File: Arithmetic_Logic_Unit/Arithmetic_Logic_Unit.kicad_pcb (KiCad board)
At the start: 2 copper layers, 95.9 x 90.2 mm, 5 parts, among them J1 PC104

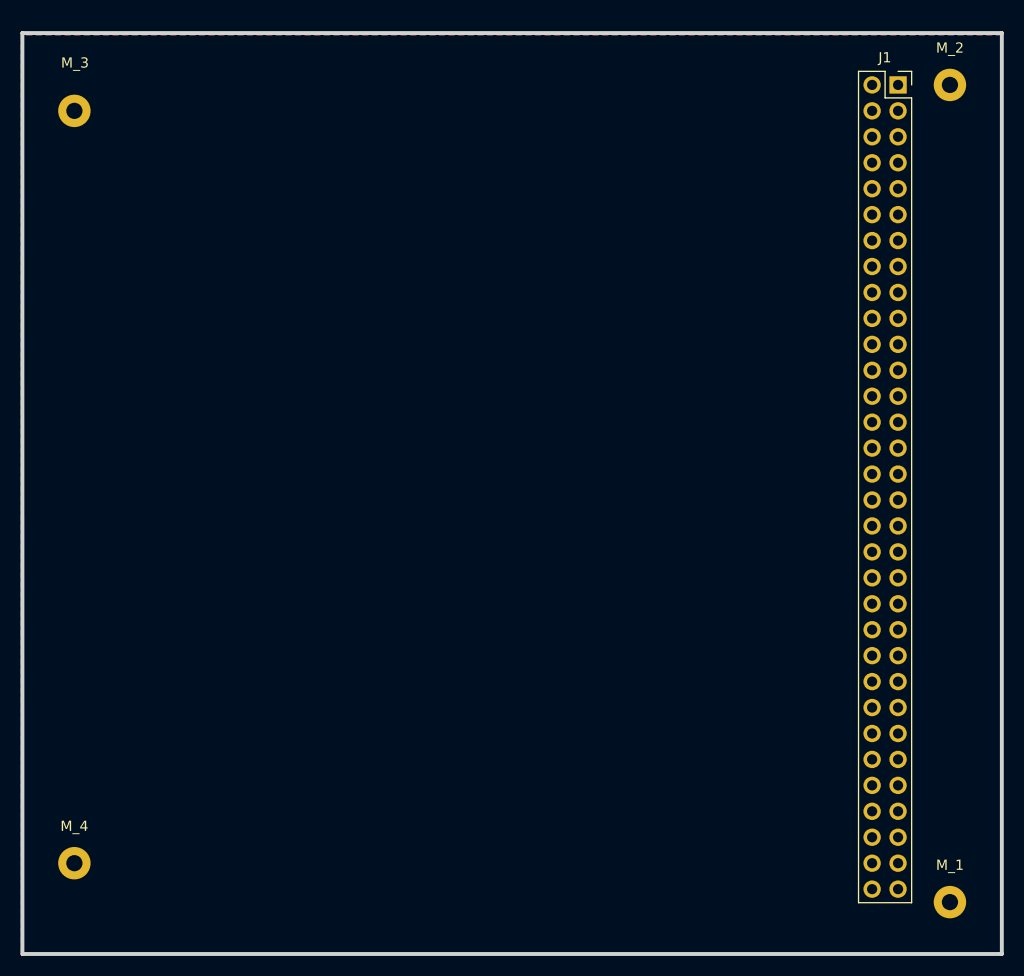
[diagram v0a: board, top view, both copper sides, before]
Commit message: preliminary board layout, will move IR to clock module
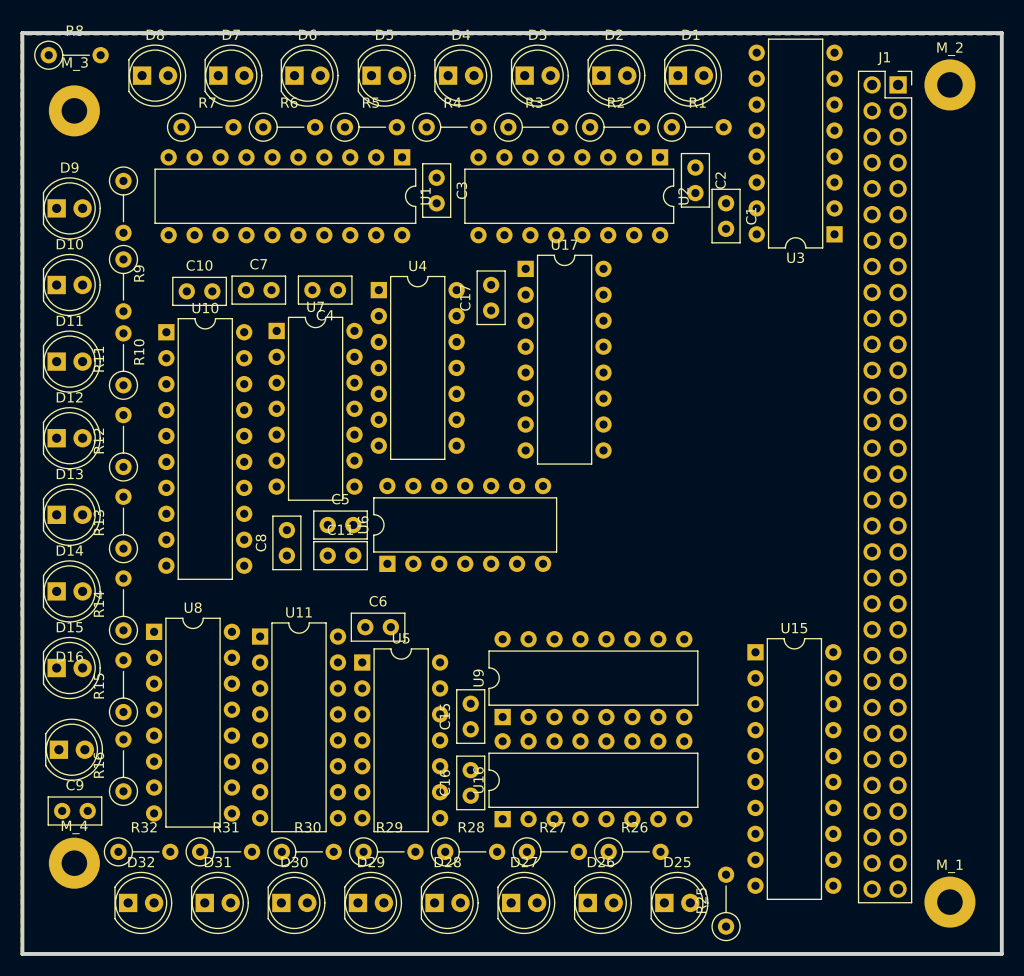
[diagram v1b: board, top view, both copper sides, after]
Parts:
- added C1: .01µF, Capacitor_THT:C_Disc_D5.0mm_W2.5mm_P2.50mm, F.Cu at (150.8, 53.5)
- added C10: .01µF, Capacitor_THT:C_Disc_D5.0mm_W2.5mm_P2.50mm, F.Cu at (98.0, 62.1)
- added C11: .01µF, Capacitor_THT:C_Disc_D5.0mm_W2.5mm_P2.50mm, F.Cu at (111.8, 88.0)
- added C15: .01µF, Capacitor_THT:C_Disc_D5.0mm_W2.5mm_P2.50mm, F.Cu at (125.8, 105.0)
- added C16: .01µF, Capacitor_THT:C_Disc_D5.0mm_W2.5mm_P2.50mm, F.Cu at (125.8, 111.5)
- added C17: .01µF, Capacitor_THT:C_Disc_D5.0mm_W2.5mm_P2.50mm, F.Cu at (127.8, 64.0)
- added C2: .01µF, Capacitor_THT:C_Disc_D5.0mm_W2.5mm_P2.50mm, F.Cu at (147.8, 50.0)
- added C3: .01µF, Capacitor_THT:C_Disc_D5.0mm_W2.5mm_P2.50mm, F.Cu at (122.5, 51.0)
- added C4: .01µF, Capacitor_THT:C_Disc_D5.0mm_W2.5mm_P2.50mm, F.Cu at (112.8, 62.0)
- added C5: .01µF, Capacitor_THT:C_Disc_D5.0mm_W2.5mm_P2.50mm, F.Cu at (111.8, 85.0)
- added C6: .01µF, Capacitor_THT:C_Disc_D5.0mm_W2.5mm_P2.50mm, F.Cu at (115.5, 95.0)
- added C7: .01µF, Capacitor_THT:C_Disc_D5.0mm_W2.5mm_P2.50mm, F.Cu at (103.8, 62.0)
- added C8: .01µF, Capacitor_THT:C_Disc_D5.0mm_W2.5mm_P2.50mm, F.Cu at (107.8, 88.0)
- added C9: .01µF, Capacitor_THT:C_Disc_D5.0mm_W2.5mm_P2.50mm, F.Cu at (85.8, 113.0)
- added D1: LED, LED_THT:LED_D5.0mm, F.Cu at (146.1, 41.0)
- added D10: LED, LED_THT:LED_D5.0mm, F.Cu at (85.3, 61.5)
- added D11: LED, LED_THT:LED_D5.0mm, F.Cu at (85.3, 69.0)
- added D12: LED, LED_THT:LED_D5.0mm, F.Cu at (85.3, 76.5)
- added D13: LED, LED_THT:LED_D5.0mm, F.Cu at (85.3, 84.0)
- added D14: LED, LED_THT:LED_D5.0mm, F.Cu at (85.3, 91.5)
- added D15: LED, LED_THT:LED_D5.0mm, F.Cu at (85.3, 99.0)
- added D16: LED, LED_THT:LED_D5.0mm, F.Cu at (85.5, 107.0)
- added D2: LED, LED_THT:LED_D5.0mm, F.Cu at (138.6, 41.0)
- added D25: LED, LED_THT:LED_D5.0mm, F.Cu at (144.8, 122.0)
- added D26: LED, LED_THT:LED_D5.0mm, F.Cu at (137.3, 122.0)
- added D27: LED, LED_THT:LED_D5.0mm, F.Cu at (129.8, 122.0)
- added D28: LED, LED_THT:LED_D5.0mm, F.Cu at (122.3, 122.0)
- added D29: LED, LED_THT:LED_D5.0mm, F.Cu at (114.8, 122.0)
- added D3: LED, LED_THT:LED_D5.0mm, F.Cu at (131.1, 41.0)
- added D30: LED, LED_THT:LED_D5.0mm, F.Cu at (107.3, 122.0)
- added D31: LED, LED_THT:LED_D5.0mm, F.Cu at (99.8, 122.0)
- added D32: LED, LED_THT:LED_D5.0mm, F.Cu at (92.3, 122.0)
- added D4: LED, LED_THT:LED_D5.0mm, F.Cu at (123.6, 41.0)
- added D5: LED, LED_THT:LED_D5.0mm, F.Cu at (116.1, 41.0)
- added D6: LED, LED_THT:LED_D5.0mm, F.Cu at (108.5, 41.0)
- added D7: LED, LED_THT:LED_D5.0mm, F.Cu at (101.1, 41.0)
- added D8: LED, LED_THT:LED_D5.0mm, F.Cu at (93.6, 41.0)
- added D9: LED, LED_THT:LED_D5.0mm, F.Cu at (85.3, 54.0)
- added R1: 220, Resistor_THT:R_Axial_DIN0207_L6.3mm_D2.5mm_P5.08mm_Vertical, F.Cu at (145.5, 46.0)
- added R10: 220, Resistor_THT:R_Axial_DIN0207_L6.3mm_D2.5mm_P5.08mm_Vertical, F.Cu at (91.8, 59.0)
- added R11: 220, Resistor_THT:R_Axial_DIN0207_L6.3mm_D2.5mm_P5.08mm_Vertical, F.Cu at (91.8, 71.3)
- added R12: 220, Resistor_THT:R_Axial_DIN0207_L6.3mm_D2.5mm_P5.08mm_Vertical, F.Cu at (91.8, 79.3)
- added R13: 220, Resistor_THT:R_Axial_DIN0207_L6.3mm_D2.5mm_P5.08mm_Vertical, F.Cu at (91.8, 87.3)
- added R14: 220, Resistor_THT:R_Axial_DIN0207_L6.3mm_D2.5mm_P5.08mm_Vertical, F.Cu at (91.8, 95.3)
- added R15: 220, Resistor_THT:R_Axial_DIN0207_L6.3mm_D2.5mm_P5.08mm_Vertical, F.Cu at (91.8, 103.3)
- added R16: 220, Resistor_THT:R_Axial_DIN0207_L6.3mm_D2.5mm_P5.08mm_Vertical, F.Cu at (91.8, 111.1)
- added R2: 220, Resistor_THT:R_Axial_DIN0207_L6.3mm_D2.5mm_P5.08mm_Vertical, F.Cu at (137.5, 46.0)
- added R25: 220, Resistor_THT:R_Axial_DIN0207_L6.3mm_D2.5mm_P5.08mm_Vertical, F.Cu at (150.8, 124.3)
- added R26: 220, Resistor_THT:R_Axial_DIN0207_L6.3mm_D2.5mm_P5.08mm_Vertical, F.Cu at (139.3, 117.0)
- added R27: 220, Resistor_THT:R_Axial_DIN0207_L6.3mm_D2.5mm_P5.08mm_Vertical, F.Cu at (131.3, 117.0)
- added R28: 220, Resistor_THT:R_Axial_DIN0207_L6.3mm_D2.5mm_P5.08mm_Vertical, F.Cu at (123.3, 117.0)
- added R29: 220, Resistor_THT:R_Axial_DIN0207_L6.3mm_D2.5mm_P5.08mm_Vertical, F.Cu at (115.3, 117.0)
- added R3: 220, Resistor_THT:R_Axial_DIN0207_L6.3mm_D2.5mm_P5.08mm_Vertical, F.Cu at (129.5, 46.0)
- added R30: 220, Resistor_THT:R_Axial_DIN0207_L6.3mm_D2.5mm_P5.08mm_Vertical, F.Cu at (107.3, 117.0)
- added R31: 220, Resistor_THT:R_Axial_DIN0207_L6.3mm_D2.5mm_P5.08mm_Vertical, F.Cu at (99.3, 117.0)
- added R32: 220, Resistor_THT:R_Axial_DIN0207_L6.3mm_D2.5mm_P5.08mm_Vertical, F.Cu at (91.3, 117.0)
- added R4: 220, Resistor_THT:R_Axial_DIN0207_L6.3mm_D2.5mm_P5.08mm_Vertical, F.Cu at (121.5, 46.0)
- added R5: 220, Resistor_THT:R_Axial_DIN0207_L6.3mm_D2.5mm_P5.08mm_Vertical, F.Cu at (113.5, 46.0)
- added R6: 220, Resistor_THT:R_Axial_DIN0207_L6.3mm_D2.5mm_P5.08mm_Vertical, F.Cu at (105.5, 46.0)
- added R7: 220, Resistor_THT:R_Axial_DIN0207_L6.3mm_D2.5mm_P5.08mm_Vertical, F.Cu at (97.5, 46.0)
- added R8: 220, Resistor_THT:R_Axial_DIN0207_L6.3mm_D2.5mm_P5.08mm_Vertical, F.Cu at (84.5, 39.0)
- added R9: 220, Resistor_THT:R_Axial_DIN0207_L6.3mm_D2.5mm_P5.08mm_Vertical, F.Cu at (91.8, 51.3)
- added U1: 74LS245, Package_DIP:DIP-20_W7.62mm, F.Cu at (119.1, 49.0)
- added U10: 74LS245, Package_DIP:DIP-20_W7.62mm, F.Cu at (96.0, 66.1)
- added U11: 74LS173, Package_DIP:DIP-16_W7.62mm, F.Cu at (105.2, 95.9)
- added U15: 74LS245, Package_DIP:DIP-20_W7.62mm, F.Cu at (153.7, 97.5)
- added U16: 74LS173, Package_DIP:DIP-16_W7.62mm, F.Cu at (128.9, 113.8)
- added U17: 74LS173, Package_DIP:DIP-16_W7.62mm, F.Cu at (131.2, 59.9)
- added U2: 74LS173, Package_DIP:DIP-16_W7.62mm, F.Cu at (144.3, 49.0)
- added U3: 74LS173, Package_DIP:DIP-16_W7.62mm, F.Cu at (161.4, 56.5)
- added U4: 74LS08, Package_DIP:DIP-14_W7.62mm, F.Cu at (116.8, 62.0)
- added U5: 74LS86, Package_DIP:DIP-14_W7.62mm, F.Cu at (115.2, 98.5)
- added U6: 74LS86, Package_DIP:DIP-14_W7.62mm, F.Cu at (117.6, 88.8)
- added U7: 74LS02, Package_DIP:DIP-14_W7.62mm, F.Cu at (106.8, 66.0)
- added U8: 74LS283, Package_DIP:DIP-16_W7.62mm, F.Cu at (94.8, 95.5)
- added U9: 74LS283, Package_DIP:DIP-16_W7.62mm, F.Cu at (128.9, 103.8)
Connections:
- J1 pad 13: unconnected-(J1-Pin_13-Pad13) -> /en_sub
- J1 pad 14: unconnected-(J1-Pin_14-Pad14) -> /clearIR
- J1 pad 15: unconnected-(J1-Pin_15-Pad15) -> /clearA
- J1 pad 16: unconnected-(J1-Pin_16-Pad16) -> /clearB
- J1 pad 17: unconnected-(J1-Pin_17-Pad17) -> /cf
- J1 pad 18: unconnected-(J1-Pin_18-Pad18) -> /zf
- J1 pad 19: unconnected-(J1-Pin_19-Pad19) -> /clear
- J1 pad 2: unconnected-(J1-Pin_2-Pad2) -> /bus7
- J1 pad 20: unconnected-(J1-Pin_20-Pad20) -> /fi
- J1 pad 21: unconnected-(J1-Pin_21-Pad21) -> /ir7
- J1 pad 22: unconnected-(J1-Pin_22-Pad22) -> /ir6
- J1 pad 23: unconnected-(J1-Pin_23-Pad23) -> /ir5
- J1 pad 24: unconnected-(J1-Pin_24-Pad24) -> /ir4
- J1 pad 25: unconnected-(J1-Pin_25-Pad25) -> /~{IR_IE}
- J1 pad 26: unconnected-(J1-Pin_26-Pad26) -> /~{A_IE}
- J1 pad 27: unconnected-(J1-Pin_27-Pad27) -> /~{B_IE}
- J1 pad 28: unconnected-(J1-Pin_28-Pad28) -> /~{ALU_OE}
- J1 pad 29: unconnected-(J1-Pin_29-Pad29) -> /~{IR_OE}
- J1 pad 3: unconnected-(J1-Pin_3-Pad3) -> /bus6
- J1 pad 30: unconnected-(J1-Pin_30-Pad30) -> /~{B_OE}
- J1 pad 31: unconnected-(J1-Pin_31-Pad31) -> /~{A_OE}
- J1 pad 4: unconnected-(J1-Pin_4-Pad4) -> /bus5
- J1 pad 45: /CLK -> /clock
- J1 pad 5: unconnected-(J1-Pin_5-Pad5) -> /bus4
- J1 pad 6: unconnected-(J1-Pin_6-Pad6) -> /bus3
- J1 pad 63: /halt -> unconnected-(J1-Pin_63-Pad63)
- J1 pad 7: unconnected-(J1-Pin_7-Pad7) -> /bus2
- J1 pad 8: unconnected-(J1-Pin_8-Pad8) -> /bus1
- J1 pad 9: unconnected-(J1-Pin_9-Pad9) -> /bus0

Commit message: layed out PCB
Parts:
- removed C15, C16, C17: .01µF, Capacitor_THT:C_Disc_D5.0mm_W2.5mm_P2.50mm
- removed D25, D26, D27, D28, D29, D30, D31, D32: LED, LED_THT:LED_D5.0mm
- removed R25, R26, R27, R28, R29, R30, R31, R32: 220, Resistor_THT:R_Axial_DIN0207_L6.3mm_D2.5mm_P5.08mm_Vertical
- removed U15: 74LS245, Package_DIP:DIP-20_W7.62mm
- removed U16, U17: 74LS173, Package_DIP:DIP-16_W7.62mm
- added C12: .01µF, Capacitor_THT:C_Disc_D5.0mm_W2.5mm_P2.50mm, F.Cu at (156.3, 90.5)
- added C13: .01µF, Capacitor_THT:C_Disc_D5.0mm_W2.5mm_P2.50mm, F.Cu at (125.8, 112.5)
- added C14: .01µF, Capacitor_THT:C_Disc_D5.0mm_W2.5mm_P2.50mm, F.Cu at (145.6, 87.1)
- added D17: LED, LED_THT:LED_D5.0mm, F.Cu at (155.3, 122.0)
- added D18: LED, LED_THT:LED_D5.0mm, F.Cu at (147.8, 122.0)
- added D19: LED, LED_THT:LED_D5.0mm, F.Cu at (140.3, 122.0)
- added D20: LED, LED_THT:LED_D5.0mm, F.Cu at (132.8, 122.0)
- added D21: LED, LED_THT:LED_D5.0mm, F.Cu at (125.3, 122.0)
- added D22: LED, LED_THT:LED_D5.0mm, F.Cu at (117.8, 122.0)
- added D23: LED, LED_THT:LED_D5.0mm, F.Cu at (110.3, 122.0)
- added D24: LED, LED_THT:LED_D5.0mm, F.Cu at (102.8, 122.0)
- added R17: 220, Resistor_THT:R_Axial_DIN0207_L6.3mm_D2.5mm_P5.08mm_Vertical, F.Cu at (141.5, 117.0)
- added R18: 220, Resistor_THT:R_Axial_DIN0207_L6.3mm_D2.5mm_P5.08mm_Vertical, F.Cu at (133.5, 117.0)
- added R19: 220, Resistor_THT:R_Axial_DIN0207_L6.3mm_D2.5mm_P5.08mm_Vertical, F.Cu at (125.5, 117.0)
- added R20: 220, Resistor_THT:R_Axial_DIN0207_L6.3mm_D2.5mm_P5.08mm_Vertical, F.Cu at (117.5, 117.0)
- added R21: 220, Resistor_THT:R_Axial_DIN0207_L6.3mm_D2.5mm_P5.08mm_Vertical, F.Cu at (109.5, 117.0)
- added R22: 220, Resistor_THT:R_Axial_DIN0207_L6.3mm_D2.5mm_P5.08mm_Vertical, F.Cu at (101.5, 117.0)
- added R23: 220, Resistor_THT:R_Axial_DIN0207_L6.3mm_D2.5mm_P5.08mm_Vertical, F.Cu at (97.8, 123.3)
- added R24: 220, Resistor_THT:R_Axial_DIN0207_L6.3mm_D2.5mm_P5.08mm_Vertical, F.Cu at (92.8, 123.3)
- added U12: 74LS245, Package_DIP:DIP-20_W7.62mm, F.Cu at (154.2, 94.2)
- added U13: 74LS173, Package_DIP:DIP-16_W7.62mm, F.Cu at (131.2, 94.8)
- added U14: 74LS173, Package_DIP:DIP-16_W7.62mm, F.Cu at (143.2, 92.3)
- moved U8 47.2 mm to (105.2, 49.4)
- moved C9 46.5 mm to (107.8, 72.0)
- moved U5 43.7 mm to (95.3, 59.5)
- moved C8 39.8 mm to (97.8, 49.5), turned to 0 degrees
- moved C10 39.3 mm to (137.3, 63.0)
- moved U7 39.0 mm to (112.8, 104.5), turned to -90 degrees
- moved C7 38.1 mm to (110.3, 99.5), turned to 180 degrees
- moved U1 37.1 mm to (152.8, 64.5), turned to 0 degrees
- moved U11 36.2 mm to (117.8, 62.0)
- moved U9 35.7 mm to (105.3, 77.0), turned to 0 degrees
- moved U10 34.3 mm to (130.3, 67.0)
- moved C5 33.6 mm to (97.8, 54.5)
- moved C11 31.6 mm to (117.8, 57.0)
- moved C3 30.4 mm to (152.8, 52.0), turned to 0 degrees
- moved U4 27.5 mm to (117.8, 89.5)
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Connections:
- D10 pad 2: /ALU/s6 -> /ALU/s1
- D11 pad 2: /ALU/s5 -> /ALU/s2
- D12 pad 2: /ALU/s4 -> /ALU/s3
- D13 pad 2: /ALU/s3 -> /ALU/s4
- D14 pad 2: /ALU/s2 -> /ALU/s5
- D15 pad 2: /ALU/s1 -> /ALU/s6
- D16 pad 2: /ALU/s0 -> /ALU/s7
- D9 pad 2: /ALU/s7 -> /ALU/s0

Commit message: updated registers and alu
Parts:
- moved C10 110.5 mm to (40.2, 10.3)
- moved C11 110.5 mm to (20.7, 4.30)
- moved C4 110.5 mm to (25.7, 31.8)
- moved C7 110.5 mm to (13.2, 46.8)
- moved D10 110.5 mm to (-11.9, 6.83)
- moved D11 110.5 mm to (-11.9, 14.3)
- moved D12 110.5 mm to (-11.9, 21.8)
- moved D13 110.5 mm to (-11.9, 29.3)
- moved D14 110.5 mm to (-11.9, 36.8)
- moved D15 110.5 mm to (-11.9, 44.3)
- moved D16 110.5 mm to (-11.7, 52.3)
- moved D9 110.5 mm to (-11.9, -0.70)
- moved R10 110.5 mm to (-5.40, 7.30)
- moved R11 110.5 mm to (-5.40, 15.3)
- moved R12 110.5 mm to (-5.40, 23.3)
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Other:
- board text added: "High - low"
